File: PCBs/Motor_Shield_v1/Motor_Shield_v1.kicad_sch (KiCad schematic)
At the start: 26 parts, among them J1 Power, J2 Digital/PWM, J3 Analog, J4 Digital/PWM, J5 Barrel_Jack, J6 Barrel_Jack, J7 Barrel_Jack

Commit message: Update PCB
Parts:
- R1, R4: value 2,7kΩ -> 1.8kΩ
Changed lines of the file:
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@@
 			)
 		)
-		(property "Value" "2,7kΩ"
+		(property "Value" "1.8kΩ"
 			(at 257.81 120.65 90)
 			(show_name no)
@@
 			)
 		)
-		(property "Value" "2,7kΩ"
+		(property "Value" "1.8kΩ"
 			(at 114.3 132.08 90)
 			(show_name no)

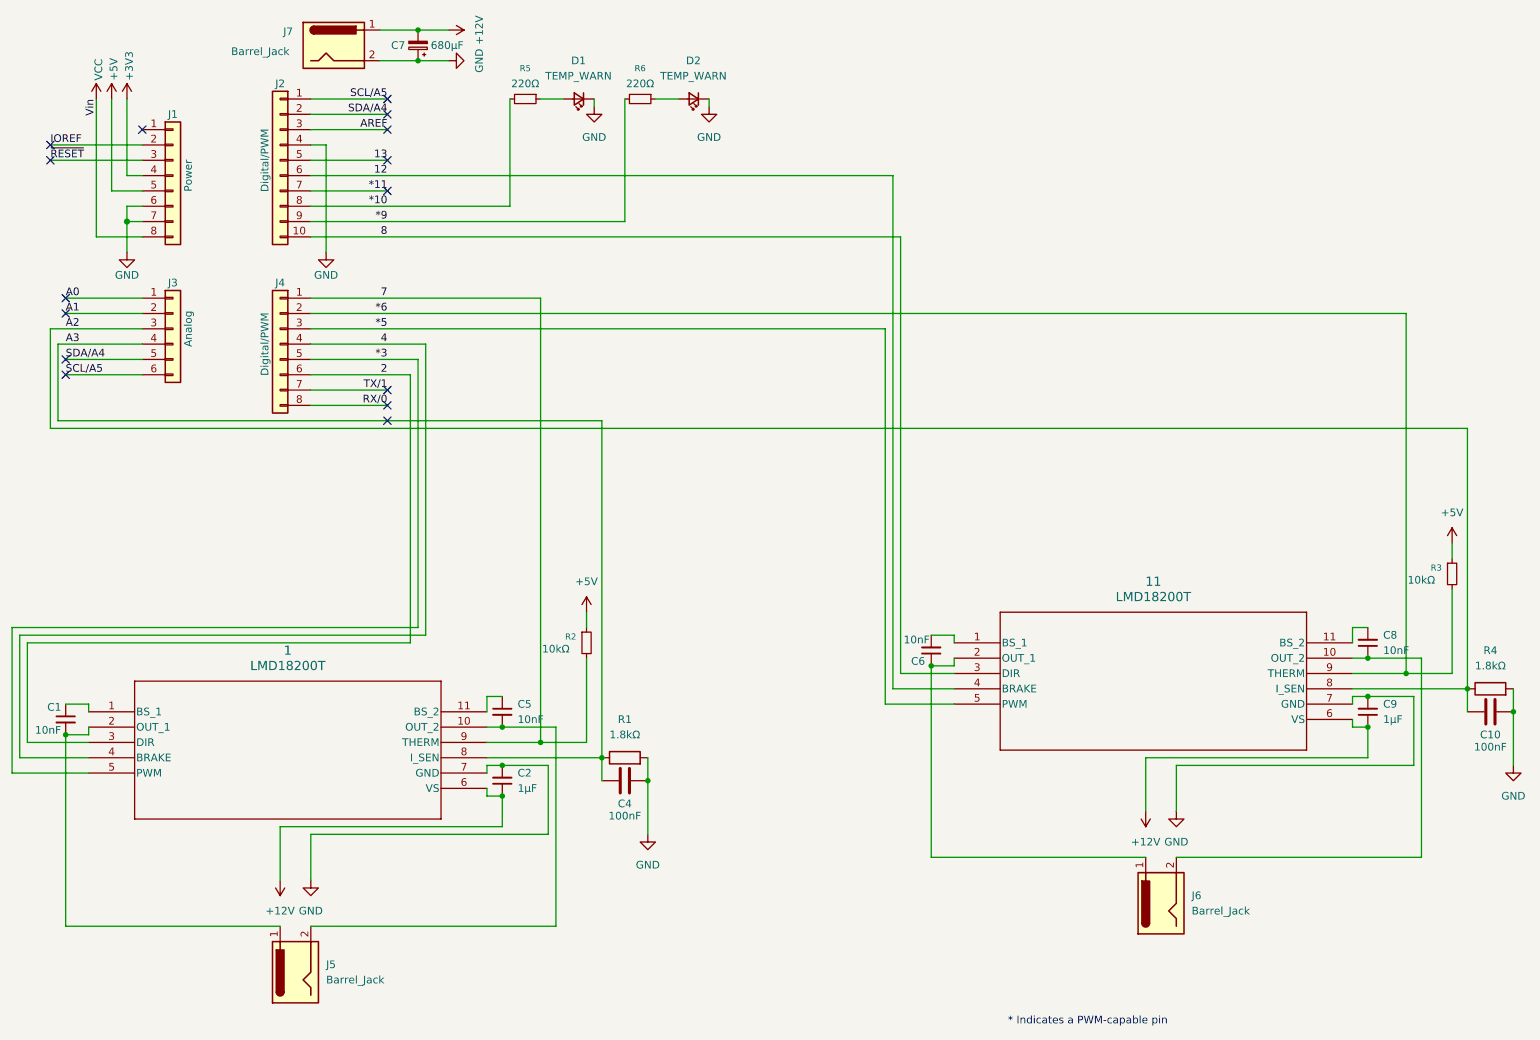
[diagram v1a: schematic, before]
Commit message: Redesign MotorShield
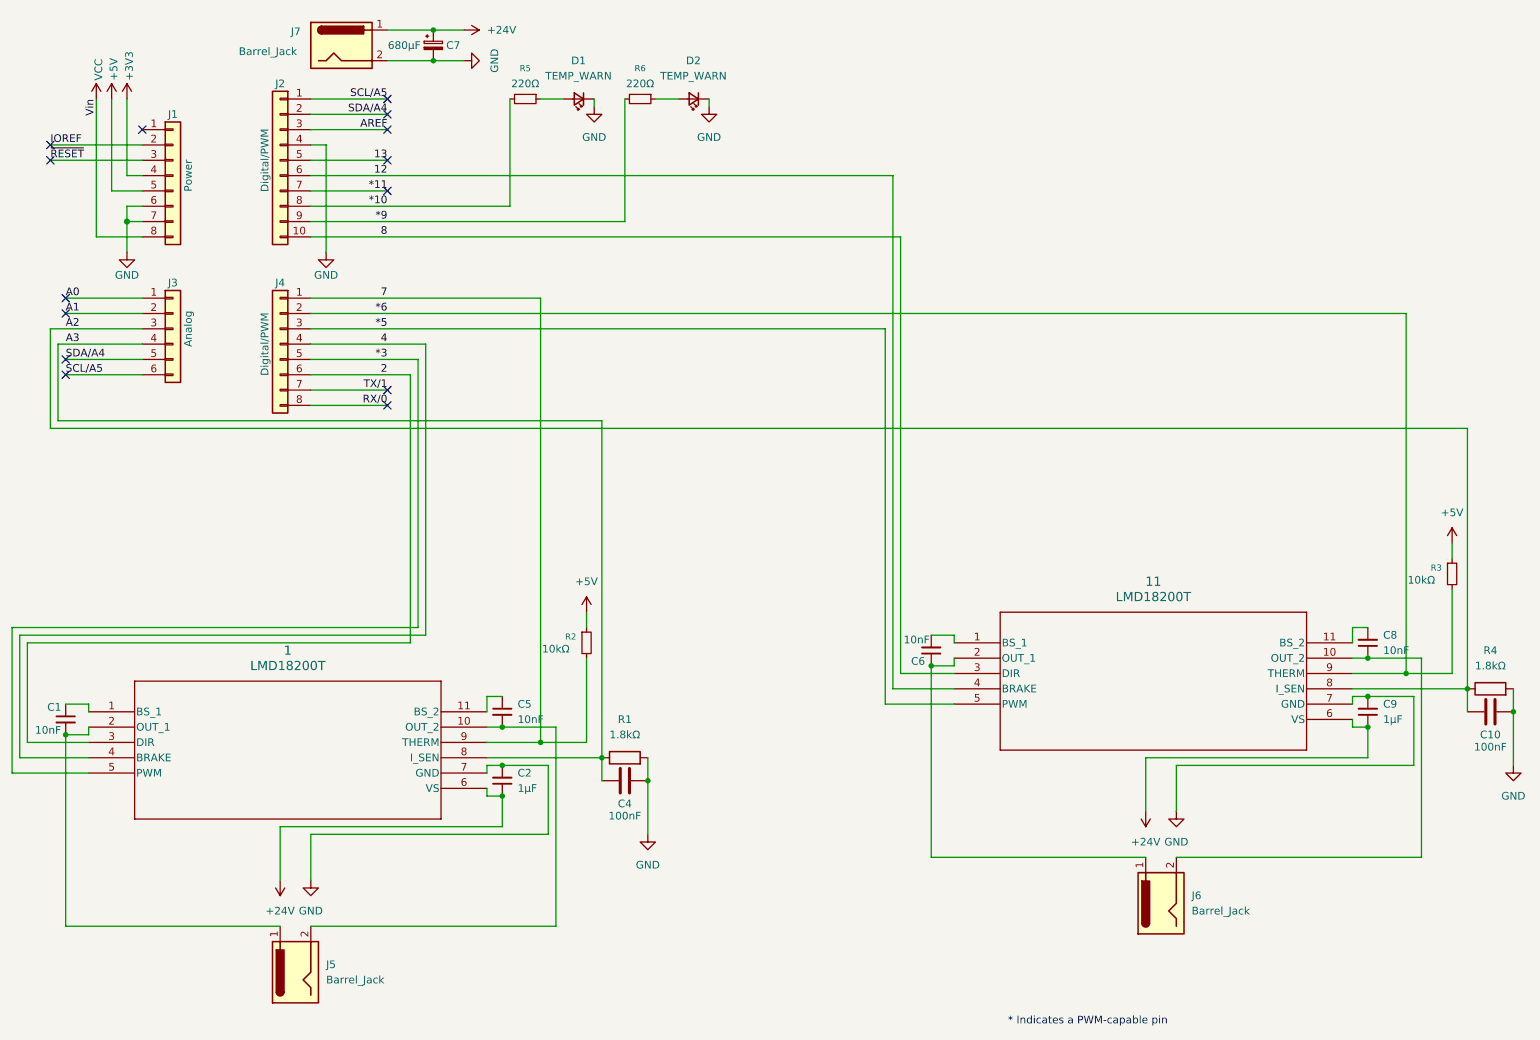
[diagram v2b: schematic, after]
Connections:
- net GND: now also C7.2; no longer C7.1
- net +12V renamed +24V
- net +24V: now also C7.1; no longer C7.2
- no-connect marks 15 -> 14
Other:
- moved on the sheet: C7, J7
